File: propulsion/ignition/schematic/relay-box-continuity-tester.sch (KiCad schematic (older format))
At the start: 7 parts, among them U3 LM393

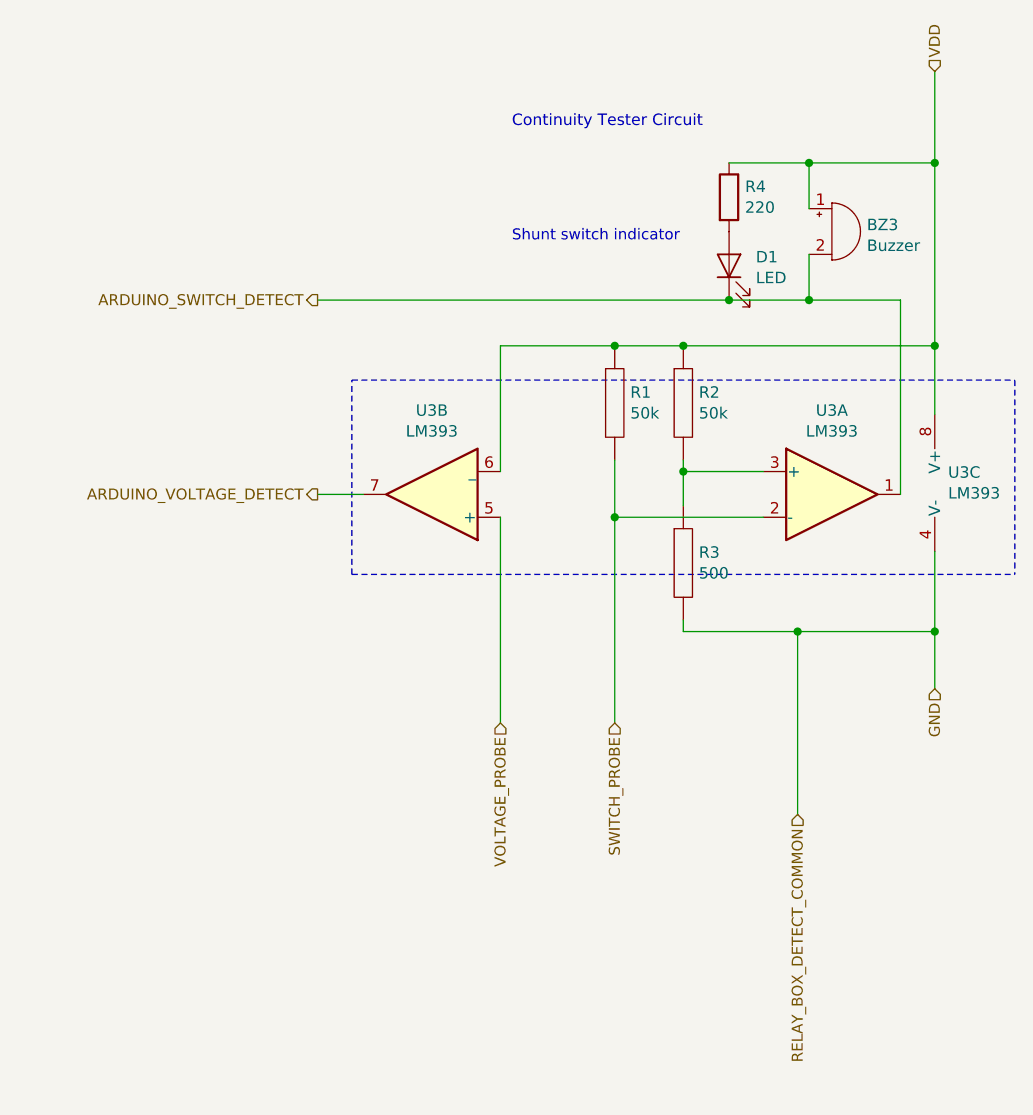
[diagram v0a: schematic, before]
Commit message: Modified continuity tester circuits for relay box, changed D6 to schottky diode, removed one relay for ball valve motor control.
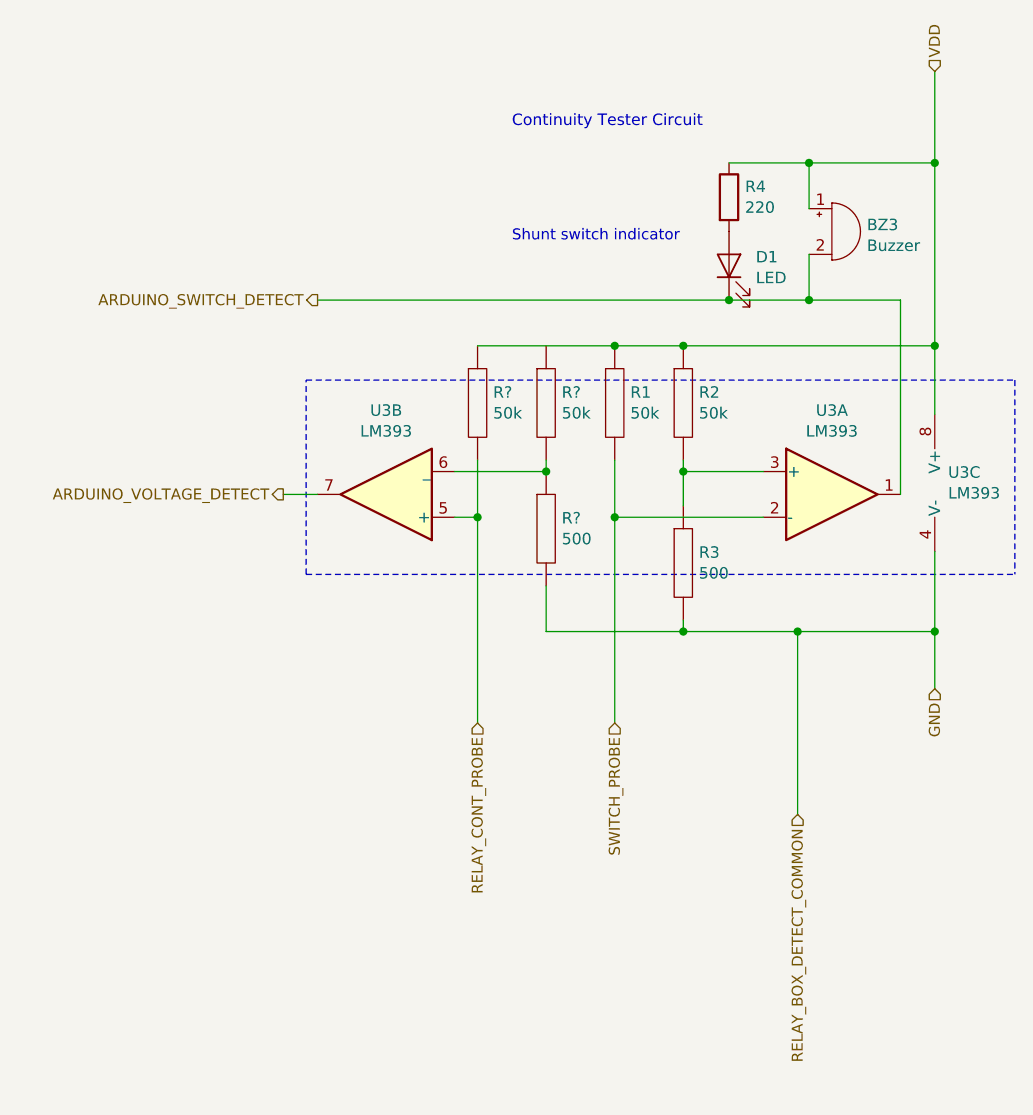
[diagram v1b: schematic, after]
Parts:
- added R? (x2): 50k, symbol pspice:R
- added R?: 500, symbol pspice:R
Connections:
- net GND: now also R?.2
- net VDD: now also R?.1; no longer U3.6 (_)
- net VOLTAGE_PROBE renamed RELAY_CONT_PROBE
- net RELAY_CONT_PROBE: now also R?.2
- new net: R?.1, R?.2, U3.6 (_)
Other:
- moved on the sheet: U3B
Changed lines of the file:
@@
 	6600 3100 6600 3950
 Wire Notes Line
-	3700 3950 3700 3100
+	3500 3950 3500 3100
 $Comp
 L pspice:R R2
@@
 L Comparator:LM393 U3
 U 2 1 5CCBEADA
-P 4050 3600
-F 0 "U3" H 4050 3233 50  0000 C CNN
-F 1 "LM393" H 4050 3324 50  0000 C CNN
-F 2 "" H 4050 3600 50  0001 C CNN
-F 3 "http://www.ti.com/lit/ds/symlink/lm393-n.pdf" H 4050 3600 50  0001 C CNN
-	2    4050 3600
+P 3850 3600
+F 0 "U3" H 3850 3233 50  0000 C CNN
+F 1 "LM393" H 3850 3324 50  0000 C CNN
+F 2 "" H 3850 3600 50  0001 C CNN
+F 3 "http://www.ti.com/lit/ds/symlink/lm393-n.pdf" H 3850 3600 50  0001 C CNN
+	2    3850 3600
 	-1   0    0    1
 $EndComp
-Wire Wire Line
-	4850 2950 4350 2950
-Wire Wire Line
-	4350 2950 4350 3500
 Connection ~ 4850 2950
 Wire Wire Line
-	4350 3700 4350 4600
-Wire Wire Line
-	3750 3600 3550 3600
-Text HLabel 3550 3600 0    48   Output ~ 0
+	4250 3700 4250 4600
+Text HLabel 3400 3600 0    48   Output ~ 0
 ARDUINO_VOLTAGE_DETECT
-Text HLabel 4350 4600 3    48   Input ~ 0
-VOLTAGE_PROBE
-Wire Notes Line
-	3700 3100 6600 3100
-Wire Notes Line
-	3700 3950 6600 3950
+Text HLabel 4250 4600 3    48   Input ~ 0
+RELAY_CONT_PROBE
 Wire Wire Line
 	4850 3450 4850 3700
@@
 Wire Wire Line
 	4850 3700 4850 4600
+Wire Wire Line
+	3400 3600 3550 3600
+$Comp
+L pspice:R R?
+U 1 1 5D54AB9F
+P 4550 3200
+F 0 "R?" H 4618 3246 50  0000 L CNN
+F 1 "50k" H 4618 3155 50  0000 L CNN
+F 2 "" H 4550 3200 50  0001 C CNN
+F 3 "~" H 4550 3200 50  0001 C CNN
+	1    4550 3200
+	1    0    0    -1
+$EndComp
+$Comp
+L pspice:R R?
+U 1 1 5D54AF3C
+P 4250 3200
+F 0 "R?" H 4318 3246 50  0000 L CNN
+F 1 "50k" H 4318 3155 50  0000 L CNN
+F 2 "" H 4250 3200 50  0001 C CNN
+F 3 "~" H 4250 3200 50  0001 C CNN
+	1    4250 3200
+	1    0    0    -1
+$EndComp
+$Comp
+L pspice:R R?
+U 1 1 5D54B313
+P 4550 3750
+F 0 "R?" H 4618 3796 50  0000 L CNN
+F 1 "500" H 4618 3705 50  0000 L CNN
+F 2 "" H 4550 3750 50  0001 C CNN
+F 3 "~" H 4550 3750 50  0001 C CNN
+	1    4550 3750
+	1    0    0    -1
+$EndComp
+Wire Wire Line
+	4550 3450 4550 3500
+Wire Wire Line
+	4550 3500 4150 3500
+Connection ~ 4550 3500
+Wire Wire Line
+	4250 3450 4250 3700
+Wire Wire Line
+	4250 3700 4150 3700
+Connection ~ 4250 3700
+Wire Wire Line
+	4550 4000 4550 4200
+Wire Wire Line
+	4550 4200 5150 4200
+Connection ~ 5150 4200
+Wire Wire Line
+	4250 2950 4850 2950
+Wire Notes Line
+	3500 3100 6600 3100
+Wire Notes Line
+	3500 3950 6600 3950
 $EndSCHEMATC
